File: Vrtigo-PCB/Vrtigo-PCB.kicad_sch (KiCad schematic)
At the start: 18 parts, among them CN1 PJ-320D, CN2 PJ-320D, Q1 2N3906, Q2 2N3906, Q3 2N3906, Q4 2N3906, Q5 2n3904, Q6 2n3904, Q7 2n3904, Q8 2n3904

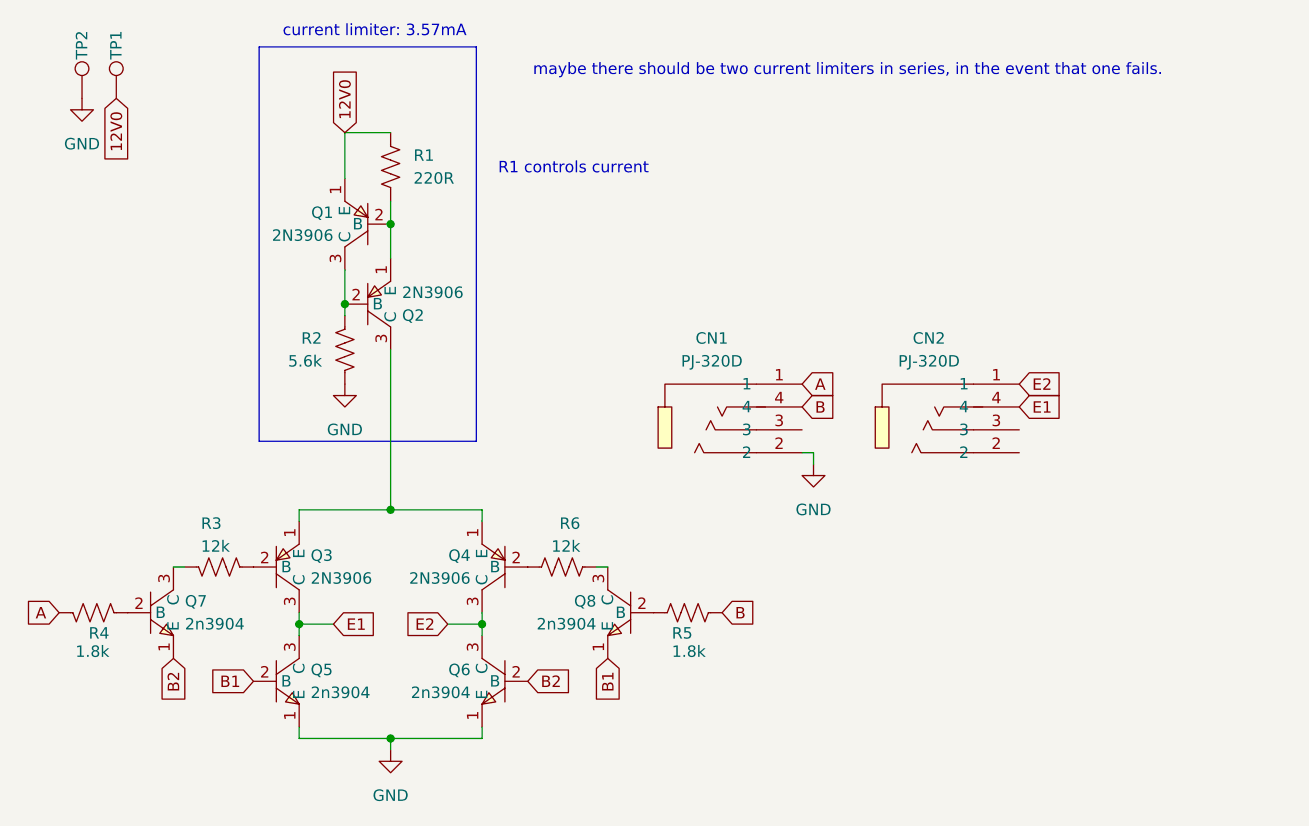
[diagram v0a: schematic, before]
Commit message: - Improved PCB layout - Added PCB silkscreen
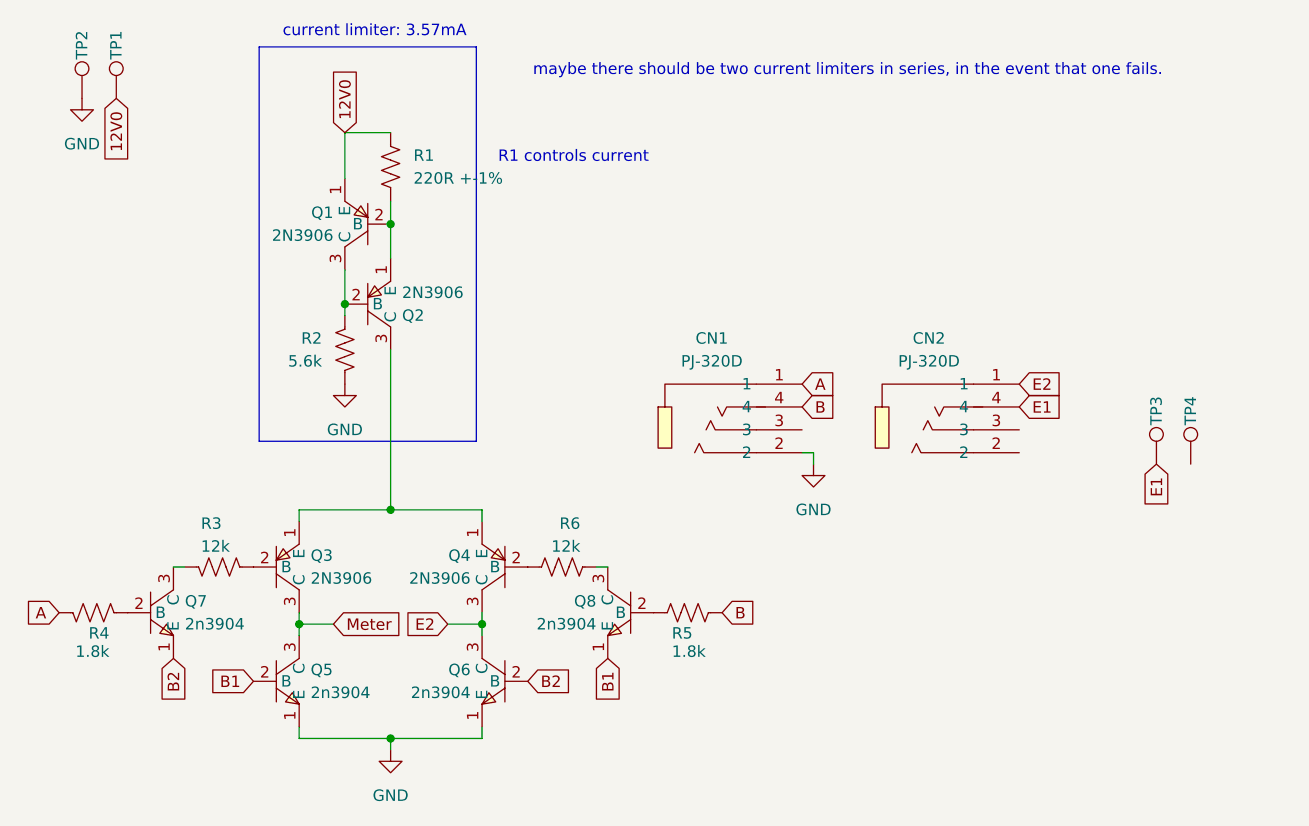
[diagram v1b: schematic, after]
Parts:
- added TP3, TP4: ~, justPads_custom:2_3-1.5_2.5_1_1, symbol Connector:TestPoint
- R1: value 220R -> 220R +-1%
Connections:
- net E1: now also TP3.1; no longer Q3.3 (C), Q5.3 (C)
- new net Meter: Q3.3 (C), Q5.3 (C)
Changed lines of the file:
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@@
 	(text "R1 controls current"
 		(exclude_from_sim no)
-		(at 143.51 62.484 0)
+		(at 143.51 61.214 0)
 		(effects
 			(font
@@
 		)
 	)
+	(global_label "E1"
+		(shape input)
+		(at 193.04 88.9 0)
+		(fields_autoplaced yes)
+		(effects
+			(font
+				(size 1.27 1.27)
+			)
+			(justify left)
+		)
+		(property "Intersheetrefs" "${INTERSHEET_REFS}"
+			(at 198.3837 88.9 0)
+			(effects
+				(font
+					(size 1.27 1.27)
+				)
+				(justify left)
+				(hide yes)
+			)
+		)
+	)
 	(global_label "B1"
 		(shape input)
@@
 		)
 	)
+	(global_label "Meter"
+		(shape input)
+		(at 116.84 113.03 0)
+		(fields_autoplaced yes)
+		(effects
+			(font
+				(size 1.27 1.27)
+			)
+			(justify left)
+		)
+		(property "Intersheetrefs" "${INTERSHEET_REFS}"
+			(at 124.9657 113.03 0)
+			(effects
+				(font
+					(size 1.27 1.27)
+				)
+				(justify left)
+				(hide yes)
+			)
+		)
+	)
 	(global_label "B1"
 		(shape input)
@@
 		)
 	)
-	(global_label "E1"
+	(global_label "B2"
 		(shape input)
-		(at 116.84 113.03 0)
+		(at 99.06 116.84 270)
 		(fields_autoplaced yes)
 		(effects
@@
 				(size 1.27 1.27)
 			)
-			(justify left)
+			(justify right)
 		)
 		(property "Intersheetrefs" "${INTERSHEET_REFS}"
-			(at 122.1837 113.03 0)
-			(effects
-				(font
-					(size 1.27 1.27)
-				)
-				(justify left)
-				(hide yes)
-			)
-		)
-	)
-	(global_label "B2"
+			(at 99.06 122.3047 90)
+			(effects
+				(font
+					(size 1.27 1.27)
+				)
+				(justify right)
+				(hide yes)
+			)
+		)
+	)
+	(global_label "B"
 		(shape input)
-		(at 99.06 116.84 270)
+		(at 168.91 88.9 0)
 		(fields_autoplaced yes)
 		(effects
@@
 				(size 1.27 1.27)
 			)
-			(justify right)
+			(justify left)
 		)
 		(property "Intersheetrefs" "${INTERSHEET_REFS}"
-			(at 99.06 122.3047 90)
-			(effects
-				(font
-					(size 1.27 1.27)
-				)
-				(justify right)
-				(hide yes)
-			)
-		)
-	)
-	(global_label "B"
+			(at 173.1652 88.9 0)
+			(effects
+				(font
+					(size 1.27 1.27)
+				)
+				(justify left)
+				(hide yes)
+			)
+		)
+	)
+	(global_label "E1"
 		(shape input)
-		(at 168.91 88.9 0)
+		(at 208.28 95.25 270)
 		(fields_autoplaced yes)
 		(effects
@@
 				(size 1.27 1.27)
 			)
-			(justify left)
+			(justify right)
 		)
 		(property "Intersheetrefs" "${INTERSHEET_REFS}"
-			(at 173.1652 88.9 0)
-			(effects
-				(font
-					(size 1.27 1.27)
-				)
-				(justify left)
+			(at 208.28 100.5937 90)
+			(effects
+				(font
+					(size 1.27 1.27)
+				)
+				(justify right)
 				(hide yes)
 			)
@@
 		)
 	)
-	(global_label "E1"
+	(global_label "E2"
 		(shape input)
-		(at 193.04 88.9 0)
+		(at 193.04 86.36 0)
 		(fields_autoplaced yes)
 		(effects
@@
 		)
 		(property "Intersheetrefs" "${INTERSHEET_REFS}"
-			(at 198.3837 88.9 0)
-			(effects
-				(font
-					(size 1.27 1.27)
-				)
-				(justify left)
-				(hide yes)
-			)
-		)
-	)
-	(global_label "E2"
-		(shape input)
-		(at 193.04 86.36 0)
-		(fields_autoplaced yes)
-		(effects
-			(font
-				(size 1.27 1.27)
-			)
-			(justify left)
-		)
-		(property "Intersheetrefs" "${INTERSHEET_REFS}"
 			(at 198.3837 86.36 0)
 			(effects
@@
 			)
 		)
-		(property "Value" "220R"
+		(property "Value" "220R +-1%"
 			(at 125.73 63.4999 0)
 			(effects
@@
 	)
 	(symbol
+		(lib_id "Connector:TestPoint")
+		(at 212.09 95.25 0)
+		(unit 1)
+		(exclude_from_sim no)
+		(in_bom yes)
+		(on_board yes)
+		(dnp no)
+		(property "Reference" "TP4"
+			(at 212.09 90.932 90)
+			(effects
+				(font
+					(size 1.27 1.27)
+				)
+				(justify left)
+			)
+		)
+		(property "Value" "~"
+			(at 214.63 93.2179 0)
+			(effects
+				(font
+					(size 1.27 1.27)
+				)
+				(justify left)
+			)
+		)
+		(property "Footprint" "justPads_custom:2_3-1.5_2.5_1_1"
+			(at 217.17 95.25 0)
+			(effects
+				(font
+					(size 1.27 1.27)
+				)
+				(hide yes)
+			)
+		)
+		(property "Datasheet" "~"
+			(at 217.17 95.25 0)
+			(effects
+				(font
+					(size 1.27 1.27)
+				)
+				(hide yes)
+			)
+		)
+		(property "Description" "test point"
+			(at 212.09 95.25 0)
+			(effects
+				(font
+					(size 1.27 1.27)
+				)
+				(hide yes)
+			)
+		)
+		(pin "1"
+		)
+		(instances
+			(project "Vrtigo-PCB"
+				(path "/a73f8acd-9f34-478f-81c4-7ca1e9b5592a"
+					(reference "TP4")
+					(unit 1)
+				)
+			)
+		)
+	)
+	(symbol
 		(lib_id "easyeda2kicadagain:2n3904S-RTK_PS_C18536")
 		(at 110.49 119.38 0)
@@
 					(unit 1)
 				)
+			)
+		)
+	)
+	(symbol
+		(lib_id "Connector:TestPoint")
+		(at 208.28 95.25 0)
+		(unit 1)
+		(exclude_from_sim no)
+		(in_bom yes)
+		(on_board yes)
+		(dnp no)
+		(property "Reference" "TP3"
+			(at 208.28 90.932 90)
+			(effects
+				(font
+					(size 1.27 1.27)
+				)
+				(justify left)
+			)
+		)
+		(property "Value" "~"
+			(at 210.82 93.2179 0)
+			(effects
+				(font
+					(size 1.27 1.27)
+				)
+				(justify left)
+			)
+		)
+		(property "Footprint" "justPads_custom:2_3-1.5_2.5_1_1"
+			(at 213.36 95.25 0)
+			(effects
+				(font
+					(size 1.27 1.27)
+				)
+				(hide yes)
+			)
+		)
+		(property "Datasheet" "~"
+			(at 213.36 95.25 0)
+			(effects
+				(font
+					(size 1.27 1.27)
+				)
+				(hide yes)
+			)
+		)
+		(property "Description" "test point"
+			(at 208.28 95.25 0)
+			(effects
+				(font
+					(size 1.27 1.27)
+				)
+				(hide yes)
+			)
+		)
+		(pin "1"
+		)
+		(instances
+			(project "Vrtigo-PCB"
+				(path "/a73f8acd-9f34-478f-81c4-7ca1e9b5592a"
+					(reference "TP3")
+					(unit 1)
+				)
